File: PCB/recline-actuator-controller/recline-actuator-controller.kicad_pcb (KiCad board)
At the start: 4 copper layers, 124 parts, among them J1 DX07S016JA1R1500, J10 1757242, J11 1757242, J12 0705530002, J13 0705530002, J14 0705530002, J15 0705530002, J2 Conn_01x03, J3 RJHSE-5381, J4 1757242, J5 1757242, J6 1757242, J7 1757242, J8 1757242, J9 1757242, M1 D24V22F5, M2 D24V22F3, Q1 PSMN7R0-60YS,115, Q2 PSMN7R0-60YS,115, Q3 PSMN7R0-60YS,115, Q4 PSMN7R0-60YS,115, Q5 PSMN7R0-60YS,115, Q6 AOD4132, Q7 AOD4132, SW1 TL3330AF260QG, SW2 TL3330AF260QG, U1 TEMPLATE, U2 RP2040, U3 MAX3535ECWI+T, U4 VNH5019ATR-E, U5 VNH5019ATR-E, X1 ABM8G-12.000MHZ-18-D2Y-T

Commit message: Actuator Control Board  MOSFET
Swapped Actuator control board MOSFET over to a more thermally efficient part
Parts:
- Q6, Q7: value AOD4132 -> BSC014N04LSIATMA1; footprint AVR-KiCAD-Lib-Transistors:TO-252-2 -> AVR-KiCAD-Lib-Transistors:PG-TDSON-8_INF
- moved J12 172.5 mm to (234.8, 105.2)
- moved J13 172.5 mm to (234.8, 117.2)
- moved J14 172.5 mm to (234.8, 129.2)
- moved J15 172.5 mm to (234.8, 141.3)
- moved J1 109.7 mm to (199.0, 114.2), turned to 180 degrees
- moved J4 106.6 mm to (211.4, 85.1), turned to 90 degrees
- moved U1 102.1 mm to (189.8, 120.0)
- moved C7 98.8 mm to (188.9, 133.5)
- moved R1 98.8 mm to (188.9, 135.5)
- moved C14 98.2 mm to (199.9, 131.8)
- moved R3 98.2 mm to (199.9, 135.0)
- moved C1 98.2 mm to (194.9, 131.8)
- moved C10 98.2 mm to (197.4, 135.0)
- moved C12 98.2 mm to (197.4, 138.2)
- moved C3 98.2 mm to (194.9, 135.0)
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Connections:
- J5 pad 1: /Motor H-Bridges/M1OUTA -> /Motor H-Bridges/M1OUTB
- J5 pad 2: /Motor H-Bridges/M1OUTB -> /Motor H-Bridges/M1OUTA
- J6 pad 1: /Motor H-Bridges/M2OUTA -> /Motor H-Bridges/M2OUTB
- J6 pad 2: /Motor H-Bridges/M2OUTB -> /Motor H-Bridges/M2OUTA
- Q6 pad 2: +24V -> /Motor H-Bridges/VMOT1
- Q6 pad 3: /Motor H-Bridges/VMOT1 -> +24V
- Q7 pad 2: +24V -> /Motor H-Bridges/VMOT2
- Q7 pad 3: /Motor H-Bridges/VMOT2 -> +24V

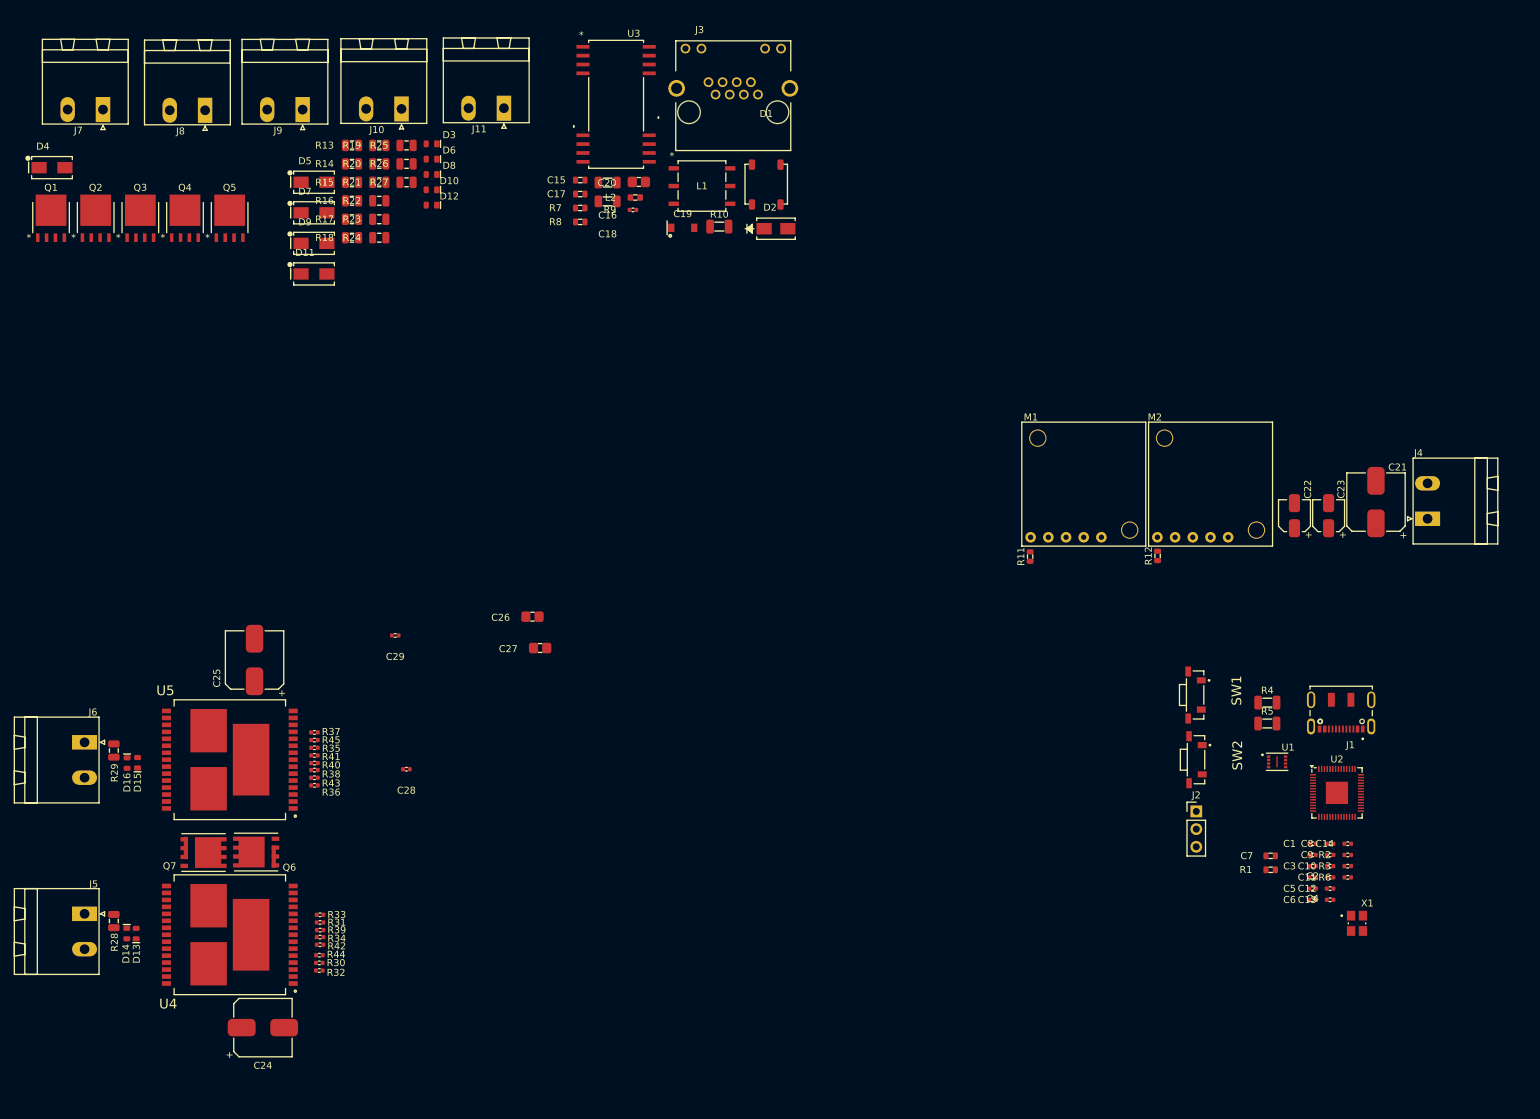
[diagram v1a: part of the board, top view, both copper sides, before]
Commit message: Switching Workstations
Syncing progress for switching to mobile workstation
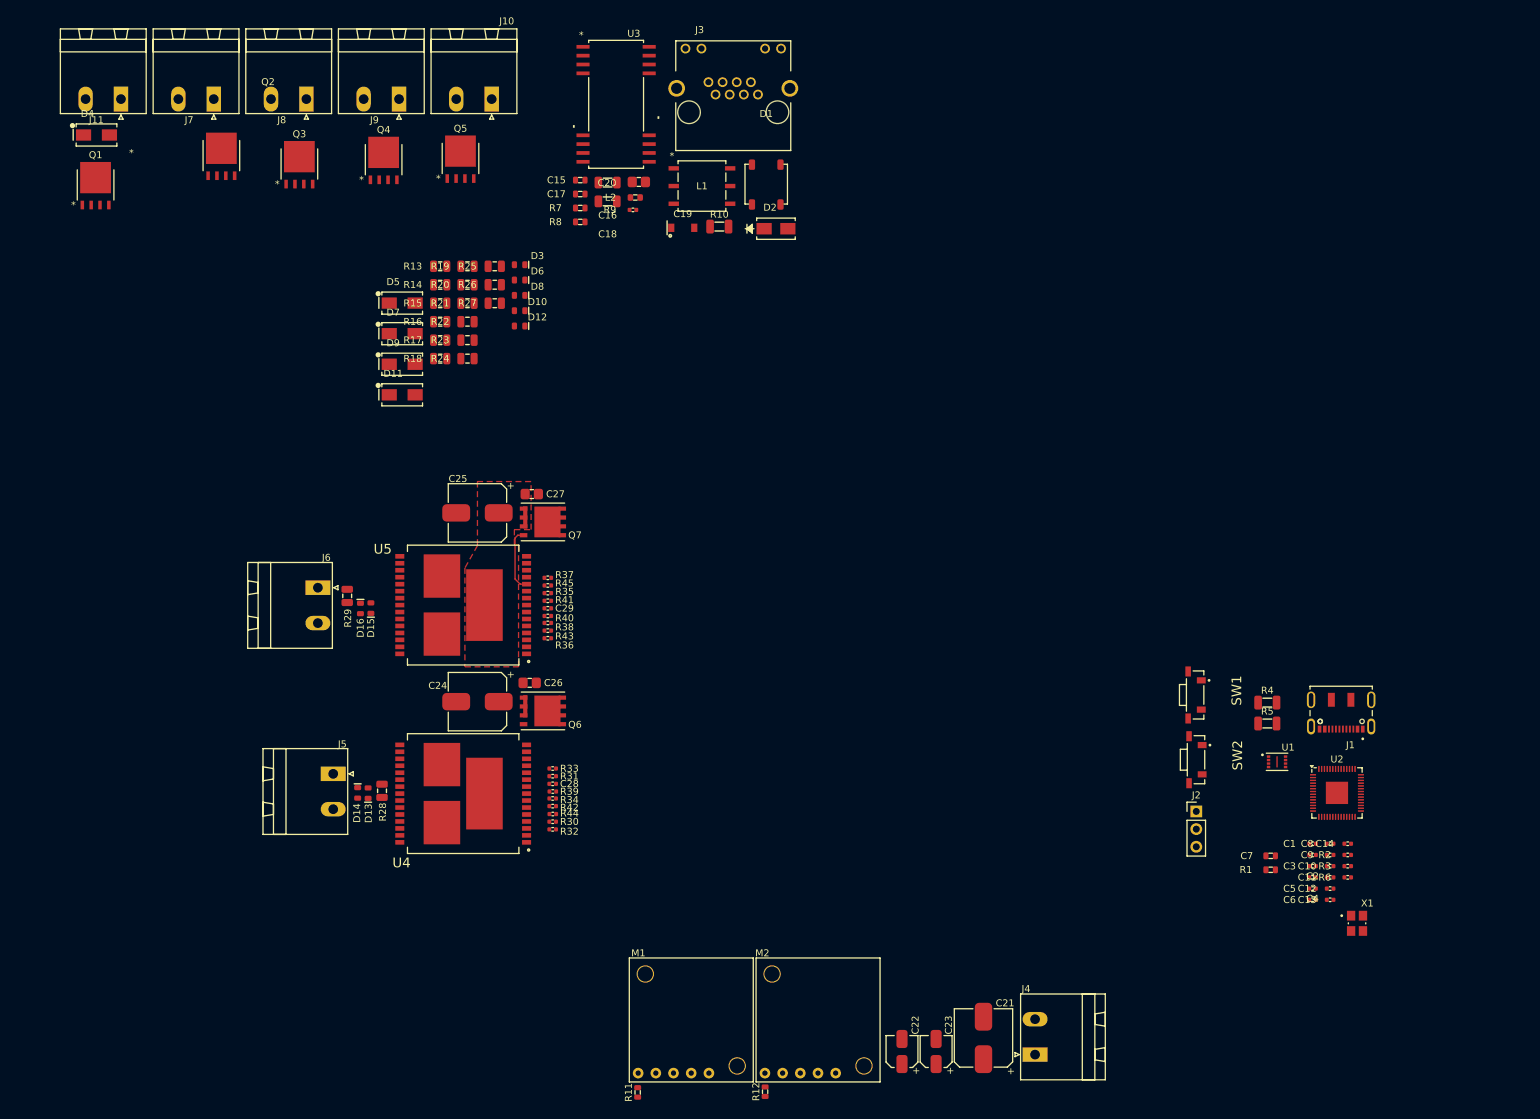
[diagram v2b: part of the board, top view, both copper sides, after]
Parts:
- moved R12 95.4 mm to (116.3, 167.4)
- moved C21 95.4 mm to (147.7, 159.7)
- moved C22 95.4 mm to (135.9, 161.6)
- moved M2 95.4 mm to (116.3, 164.7)
- moved R11 95.4 mm to (98.0, 167.5)
- moved C23 95.4 mm to (140.8, 161.6)
- moved J4 95.4 mm to (155.1, 162.1)
- moved M1 95.4 mm to (98.1, 164.7)
- moved Q7 68.0 mm to (84.4, 85.6)
- moved C24 56.0 mm to (75.0, 111.4), turned to 180 degrees
- moved J11 55.0 mm to (23.8, 24.9)
- moved Q6 45.9 mm to (84.4, 112.7), turned to 0 degrees
- moved R28 42.8 mm to (61.3, 124.2)
- moved J5 41.0 mm to (54.3, 121.8)
- moved D15 40.2 mm to (59.7, 98.0)
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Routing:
- net Net-(Q7-G): track 0.00 -> 9.24 mm
- added copper zone on F.Cu, net /Motor H-Bridges/VMOT2

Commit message: PCB shape and Layout
PCB shape defined, parts placed 90% layout in progress.
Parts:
- moved J15 176.8 mm to (63.1, 99.0), turned to 180 degrees
- moved J12 173.8 mm to (63.1, 132.0), turned to 180 degrees
- moved J14 172.8 mm to (63.1, 110.0), turned to 180 degrees
- moved J13 171.7 mm to (63.1, 121.0), turned to 180 degrees
- moved J1 146.3 mm to (55.5, 85.8), turned to -90 degrees
- moved R5 132.0 mm to (60.5, 81.8)
- moved R4 130.2 mm to (60.0, 89.8)
- moved C13 129.8 mm to (80.5, 83.5), turned to -90 degrees
- moved R2 128.6 mm to (78.0, 92.5)
- moved C9 127.4 mm to (78.0, 89.0)
- moved C8 122.3 mm to (80.8, 95.0), turned to 90 degrees
- moved R6 121.7 mm to (89.2, 86.0), turned to 180 degrees
- moved C14 121.4 mm to (84.2, 95.0), turned to 90 degrees
- moved U2 120.3 mm to (83.3, 89.5), turned to 90 degrees
- moved U1 119.9 mm to (73.5, 90.8), turned to 90 degrees
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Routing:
- net /RS485 Transceiver/A_RS485: track 0.00 -> 54.6 mm
- net /RS485 Transceiver/B_RS485: track 0.00 -> 49.3 mm
- net /RS485 Transceiver/Y_RS485: track 0.00 -> 41.8 mm
- net /RS485 Transceiver/Z_RS485: track 0.00 -> 36.1 mm
- net Net-(J3-Pad10): track 0.00 -> 30.0 mm
- net /Motor H-Bridges/VMOT2: track 0.00 -> 18.0 mm
- net Net-(U5-ENA/DIAGA): track 0.00 -> 11.1 mm
- net Net-(U3-ST1): track 0.00 -> 10.8 mm
- net Net-(Q6-G): track 0.00 -> 9.39 mm
- net Earth: track 0.00 -> 6.70 mm, vias 0 -> 5
- net Net-(U4-ENA/DIAGA): track 0.00 -> 6.37 mm
- net Net-(U3-ST2): track 0.00 -> 5.50 mm
- net Net-(U4-CS): track 0.00 -> 4.47 mm
- net Net-(U5-INB): track 0.00 -> 4.45 mm
- net Net-(U5-CS): track 0.00 -> 4.43 mm
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- added copper zone on F.Cu, net +24V
- added copper zone on F.Cu, net +3.3V
- added copper zone on F.Cu, net +5V
- added copper zone on F.Cu, net /Motor H-Bridges/VMOT1
- added copper zone on B.Cu, net /RS485 Transceiver/RJ45_SHIELD
- added copper zone on F.Cu, net /RS485 Transceiver/RJ45_SHIELD
- added copper zone on B.Cu, net Earth
- added copper zone on In1.Cu, net GND
- added copper zone on F.Cu, net Net-(Q1-D)
- added copper zone on F.Cu, net Net-(Q2-D)
- added copper zone on F.Cu, net Net-(Q3-D)
- added copper zone on F.Cu, net Net-(Q4-D)
- added copper zone on F.Cu, net Net-(Q5-D)
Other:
- board outline added: 140 x 100 mm

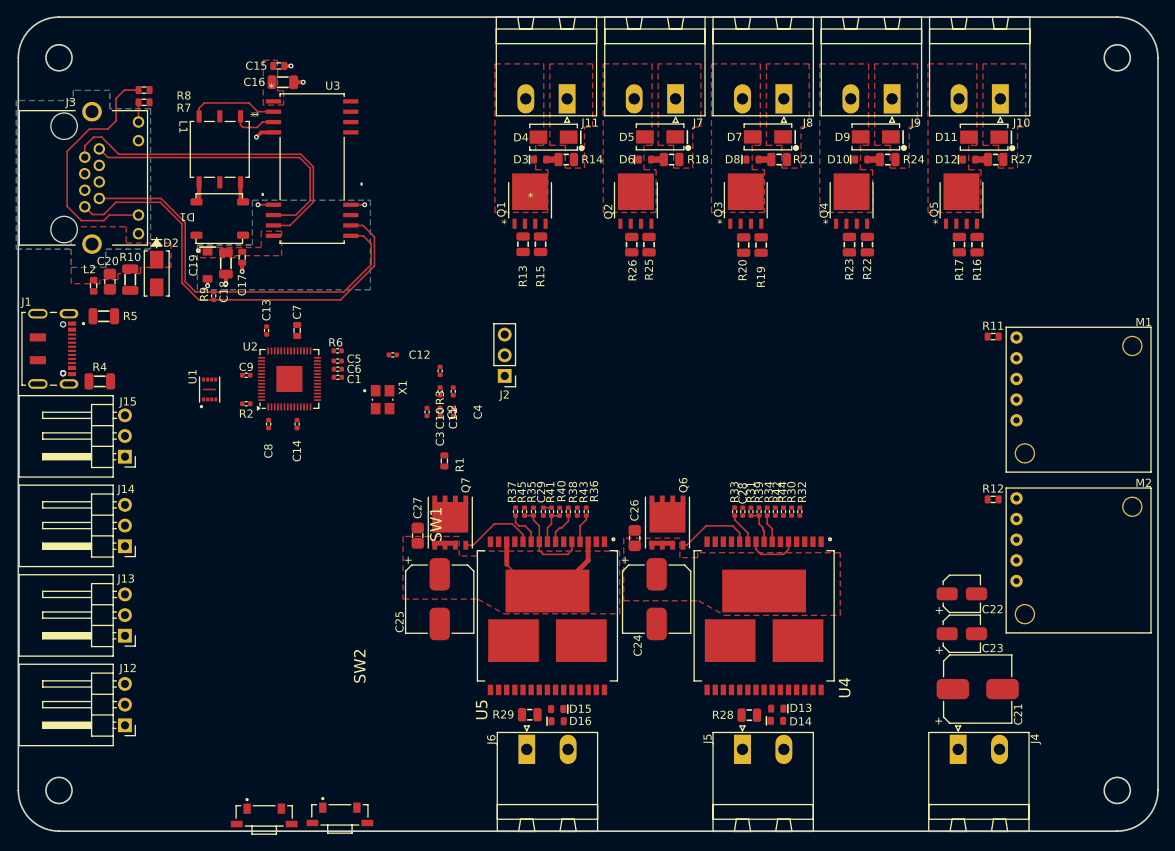
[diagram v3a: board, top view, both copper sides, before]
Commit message: PCB Layout Progress
Lots of progress made on PCB layout, MOSFET section complete, H-Bridges in progress, lots of work done and lots more to do, 3 copper layers are being utilized to provide ample copper for carrying all the current through he drivers and actuators.
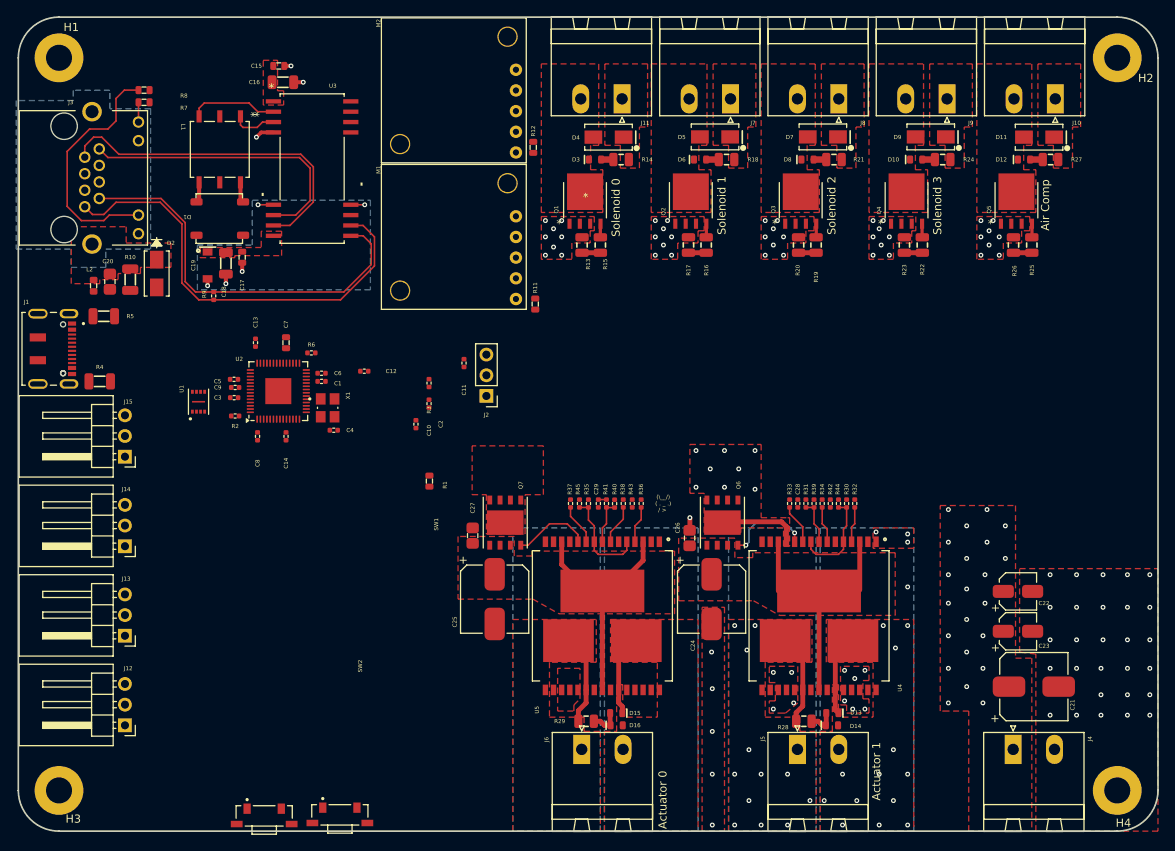
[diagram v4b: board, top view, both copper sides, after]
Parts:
- added H1: M3_Plated_Hole, AVR-KiCAD-Lib-Holes_Fasteners:M3_HOLE, F.Cu at (55.0, 50.0)
- added H2: M3_Plated_Hole, AVR-KiCAD-Lib-Holes_Fasteners:M3_HOLE, F.Cu at (185.0, 50.0)
- added H3: M3_Plated_Hole, AVR-KiCAD-Lib-Holes_Fasteners:M3_HOLE, F.Cu at (55.0, 140.0)
- added H4: M3_Plated_Hole, AVR-KiCAD-Lib-Holes_Fasteners:M3_HOLE, F.Cu at (185.0, 140.0)
- moved M2 74.7 mm to (111.1, 61.6), turned to 90 degrees
- moved R12 71.2 mm to (113.2, 61.0), turned to 90 degrees
- moved M1 61.7 mm to (111.1, 79.6), turned to 90 degrees
- moved R11 56.4 mm to (113.5, 80.2), turned to -90 degrees
- moved R25 47.0 mm to (174.5, 73.0)
- moved R26 46.9 mm to (172.2, 73.0)
- moved R16 33.3 mm to (134.5, 73.0)
- moved R17 33.3 mm to (132.3, 73.0)
- moved C3 25.4 mm to (76.5, 91.8), turned to 0 degrees
- moved C4 14.8 mm to (88.8, 95.8), turned to 180 degrees
- moved C5 12.9 mm to (76.5, 89.5), turned to 0 degrees
- moved R15 7.35 mm to (121.5, 73.0)
- moved D15 7.27 mm to (123.5, 130.5)
- moved D16 7.27 mm to (123.5, 132.0)
- moved R13 7.25 mm to (119.2, 73.0)
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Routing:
- net /Motor H-Bridges/VMOT1: track 0.00 -> 34.2 mm
- net /Motor H-Bridges/VMOT2: track 18.0 -> 30.1 mm
- net /Motor H-Bridges/M2OUTB: track 0.00 -> 11.2 mm
- net /Motor H-Bridges/M1OUTB: track 0.00 -> 11.1 mm, vias 0 -> 12
- net +24V: track 0.00 -> 10.0 mm, vias 0 -> 30
- net /Motor H-Bridges/M2OUTA: track 0.00 -> 9.98 mm
- net /Motor H-Bridges/M1OUTA: track 0.00 -> 9.96 mm, vias 0 -> 17
- net Net-(U4-ENA/DIAGA): track 6.37 -> 11.7 mm
- net Net-(U4-INA): track 0.00 -> 4.38 mm
- net Net-(D15-Pad1): track 0.00 -> 3.78 mm
- net Net-(D13-Pad1): track 0.00 -> 3.48 mm
- net /RP2040/SOLENOID_0: track 0.00 -> 2.25 mm
- net /RP2040/AIR_COMP: track 0.00 -> 2.25 mm
- net /RP2040/SOLENOID_3: track 0.00 -> 2.20 mm
- net /RP2040/SOLENOID_1: track 0.00 -> 2.18 mm
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- added copper zone on In2.Cu, net +24V
- added copper zone on In2.Cu, net +3.3V
- added copper zone on In2.Cu, net +5V
- added copper zone on B.Cu, net /Motor H-Bridges/M1OUTA
- added copper zone on F.Cu, net /Motor H-Bridges/M1OUTA
- added copper zone on In2.Cu, net /Motor H-Bridges/M1OUTA
- added copper zone on B.Cu, net /Motor H-Bridges/M1OUTB
- added copper zone on F.Cu, net /Motor H-Bridges/M1OUTB
- added copper zone on In2.Cu, net /Motor H-Bridges/M1OUTB
- added copper zone on B.Cu, net /Motor H-Bridges/M2OUTA
- added copper zone on F.Cu, net /Motor H-Bridges/M2OUTA
- added copper zone on In2.Cu, net /Motor H-Bridges/M2OUTA
- added copper zone on B.Cu, net /Motor H-Bridges/M2OUTB
- added copper zone on F.Cu, net /Motor H-Bridges/M2OUTB
- added copper zone on In2.Cu, net /Motor H-Bridges/M2OUTB
- added copper zone on F.Cu, net GND
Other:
- outline, holes or cut-outs redrawn
- board text added: "(\__/) ( . _ .) / >"
- board text added: "Actuator 0"
- board text added: "Actuator 1"
- board text added: "Air Comp"
- board text added: "Solenoid 0"
- board text added: "Solenoid 1"
- board text added: "Solenoid 2"
- board text added: "Solenoid 3"
